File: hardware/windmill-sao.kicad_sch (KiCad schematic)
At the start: 0 parts

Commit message: Add space-sensitive components to the PCB
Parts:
- added J1: Conn_02x03_Counter_Clockwise, symbol Connector_Generic:Conn_02x03_Counter_Clockwise
- added J2: Conn_01x03, symbol Connector_Generic:Conn_01x03
- added LED1: WS2812B-2020, jlcpcb-parts:LED-SMD_4P-L2.0-W2.0-TL_WS2812B-2020, symbol jlcpcb-parts:WS2812B-2020

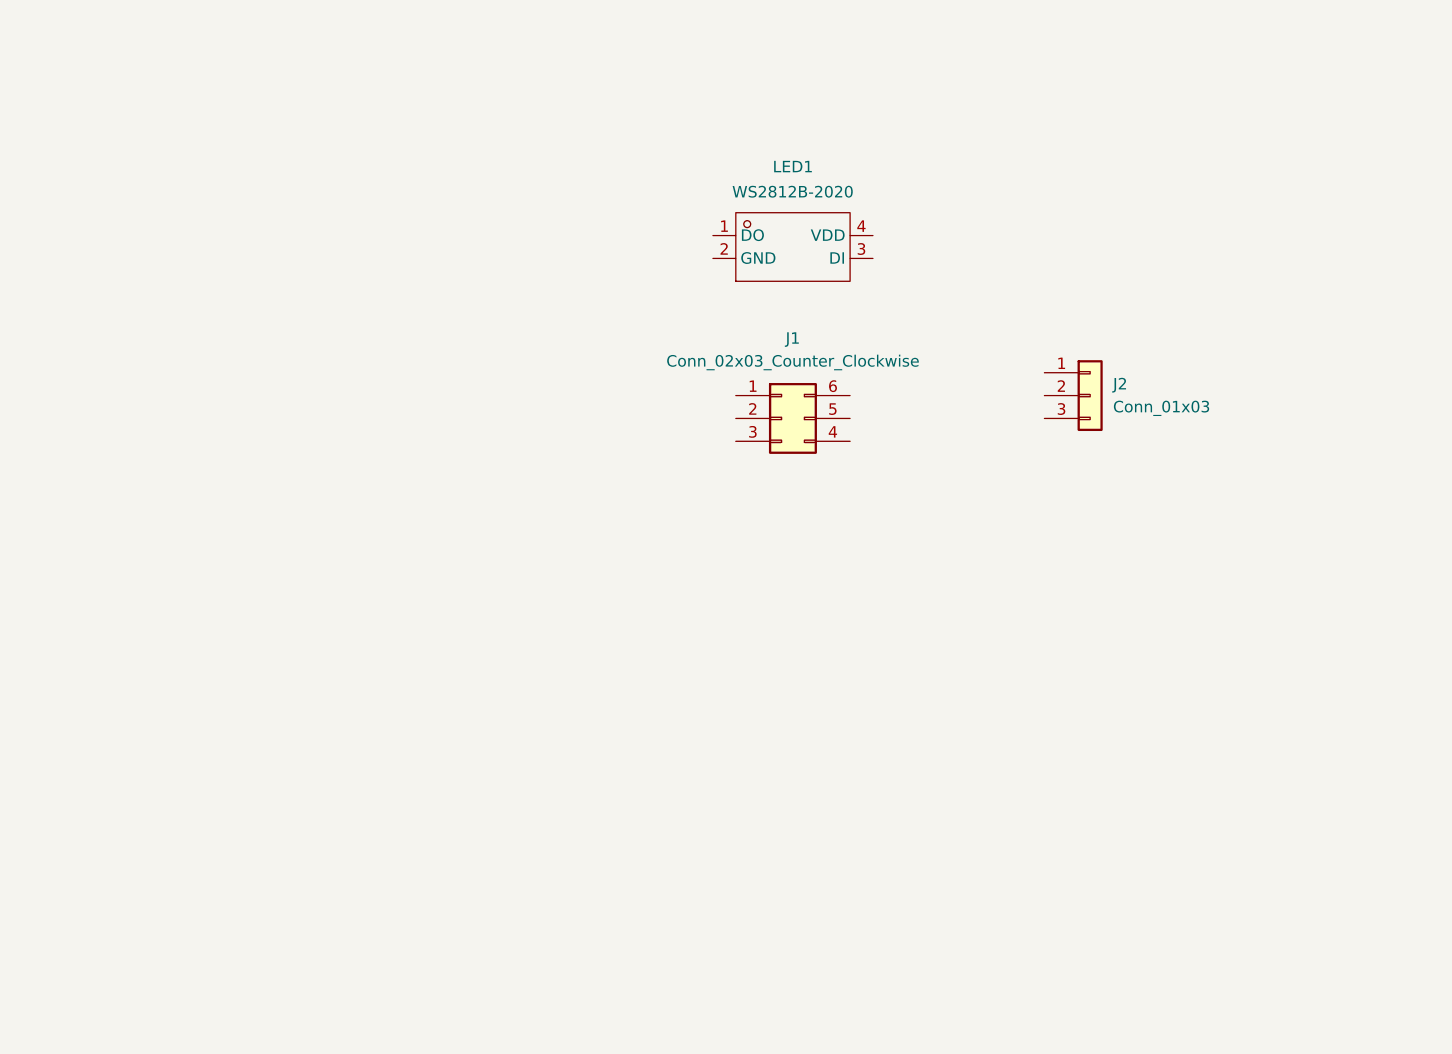
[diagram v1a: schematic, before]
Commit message: Add main PCB components
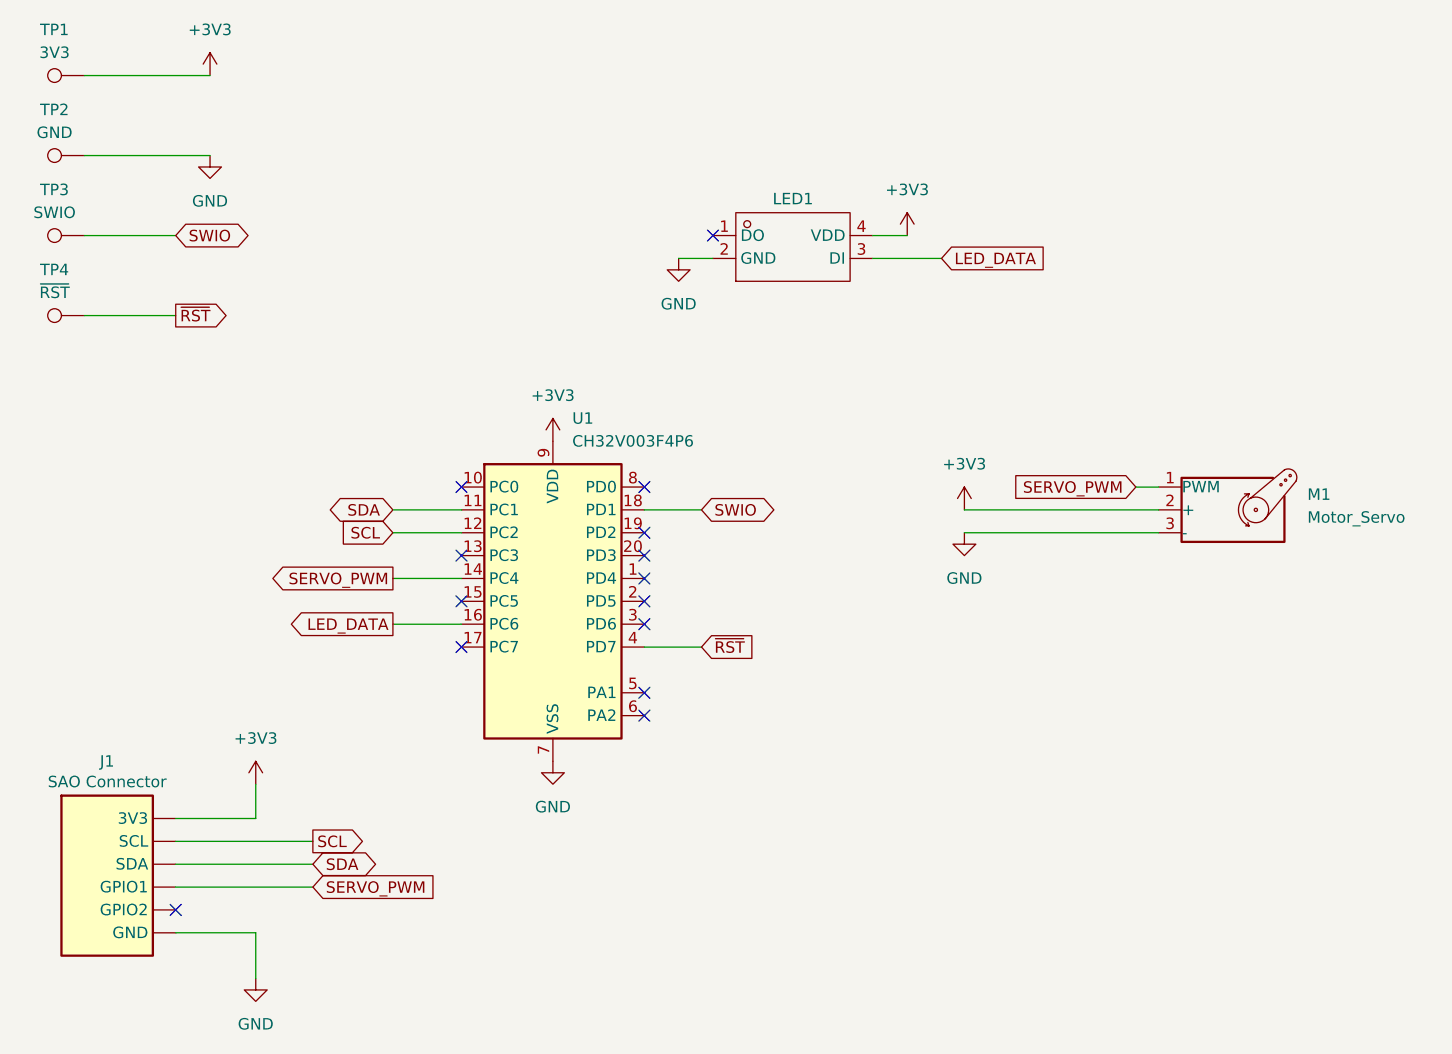
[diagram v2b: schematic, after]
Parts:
- added TP1: 3V3, TestPoint:TestPoint_Pad_D1.5mm, symbol Connector:TestPoint
- added TP2: GND, TestPoint:TestPoint_Pad_D1.5mm, symbol Connector:TestPoint
- added TP3: SWIO, TestPoint:TestPoint_Pad_D1.5mm, symbol Connector:TestPoint
- added TP4: ~{RST}, TestPoint:TestPoint_Pad_D1.5mm, symbol Connector:TestPoint
- added U1: CH32V003F4P6, Package_SO:TSSOP-20_4.4x6.5mm_P0.65mm, symbol MCU_WCH_RiscV:CH32V003FxPx
- J1: value Conn_02x03_Counter_Clockwise -> SAO Connector; footprint (none) -> kantoniak-kicad:SAO_Header_Addon_Side; symbol Connector_Generic:Conn_02x03_Counter_Clockwise -> kantoniak-kicad:Conn_SAO
- LED1: value WS2812B-2020 -> (none)
- M1: renamed from J2; value Conn_01x03 -> Motor_Servo; footprint (none) -> kantoniak-kicad:PinHeader_1x03_P2.54mm_Vertical_SG90; symbol Connector_Generic:Conn_01x03 -> Motor:Motor_Servo
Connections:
- net GND: now reaches J1.1 (GND)
- net GND: now also LED1.2 (GND), M1.3 (-), TP2.1, U1.7 (VSS)
- net SCL: now reaches J1.2 (SCL)
- net SCL: now also U1.12 (PC2)
- net SERVO_PWM: now reaches J1.4 (GPIO1)
- net SERVO_PWM: now also M1.1 (PWM), U1.14 (PC4)
- net SDA: now reaches J1.5 (SDA)
- net SDA: now also U1.11 (PC1)
- net +3V3: now reaches J1.6 (3V3)
- net +3V3: now also LED1.4 (VDD), M1.2 (+), TP1.1, U1.9 (VDD)
- net LED_DATA: now reaches LED1.3 (DI)
- net LED_DATA: now also U1.16 (PC6)
- new net SWIO: TP3.1, U1.18 (PD1)
- new net ~{RST}: TP4.1, U1.4 (PD7)
- no-connect marks 0 -> 14

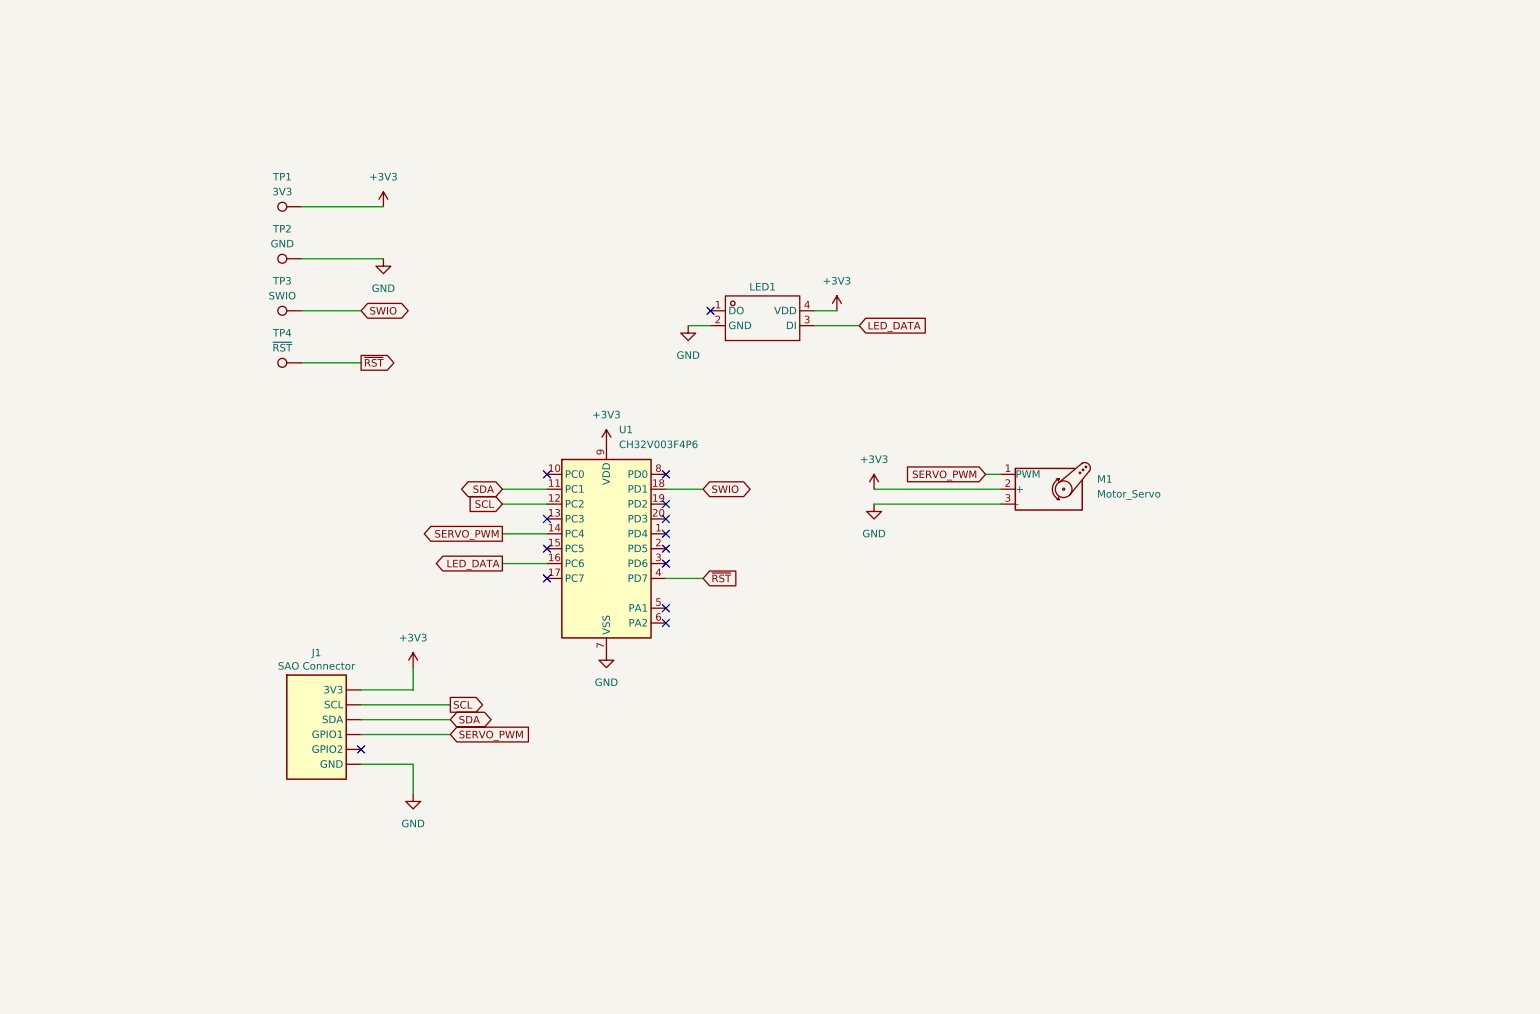
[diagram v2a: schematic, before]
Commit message: Add passives to the schematic, PCB WIP
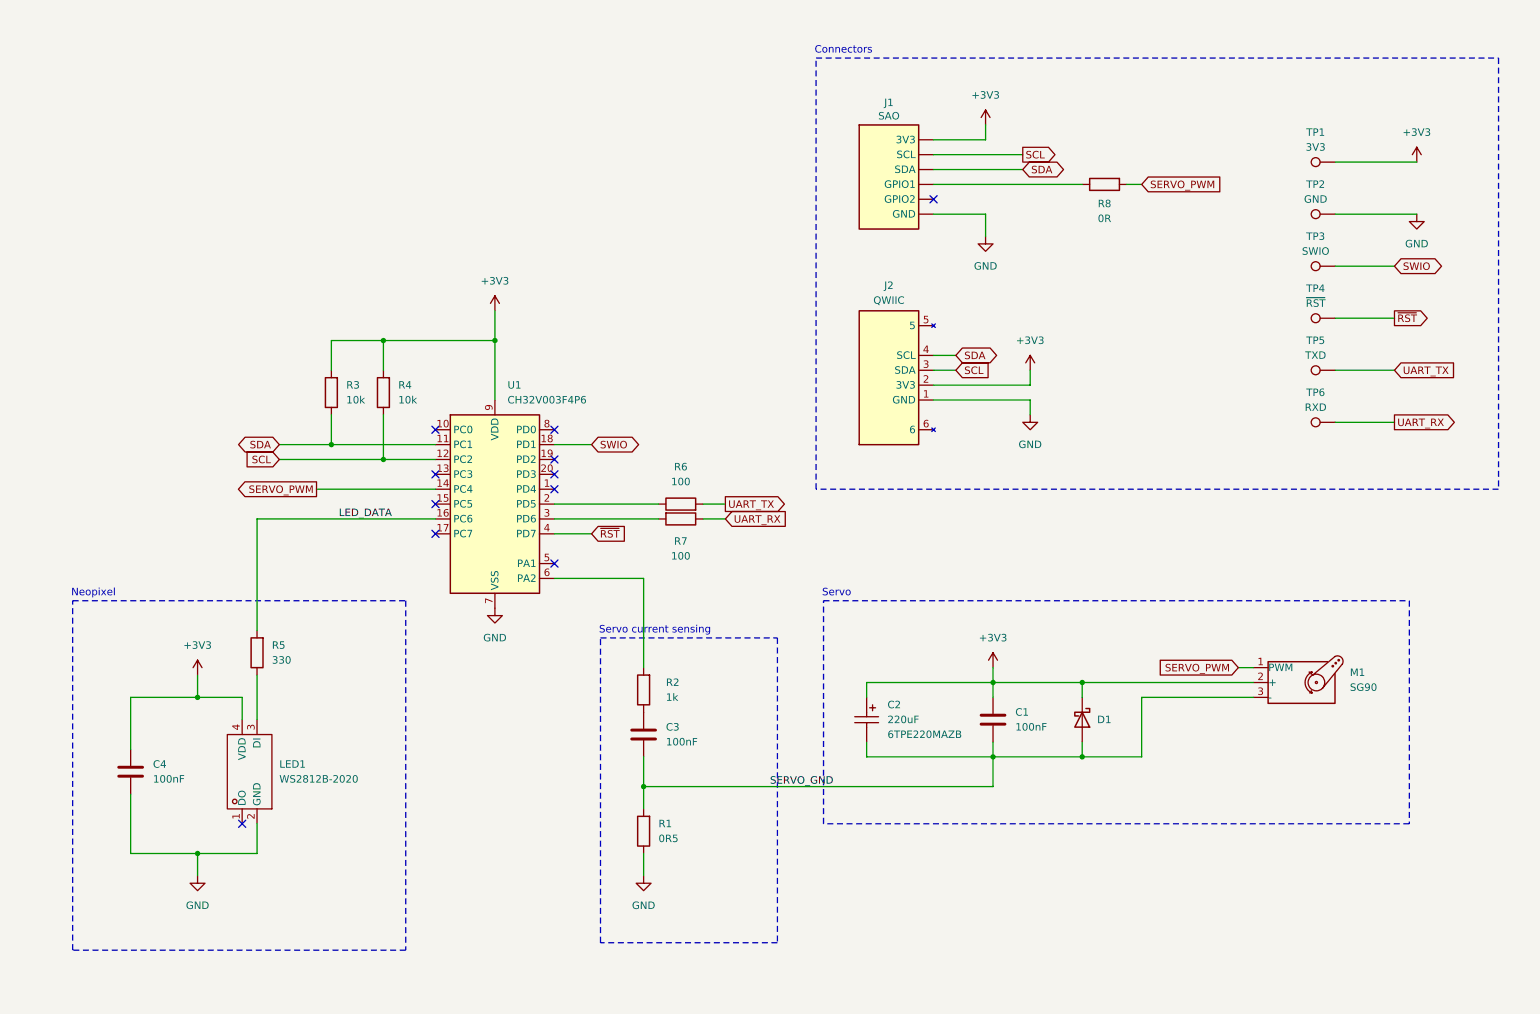
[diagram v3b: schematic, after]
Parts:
- added C1, C3, C4: 100nF, Capacitor_SMD:C_0201_0603Metric_Pad0.64x0.40mm_HandSolder, symbol Device:C
- added C2: 220uF, Capacitor_Tantalum_SMD:CP_EIA-3528-21_Kemet-B_HandSolder, symbol jlcpcb-parts:6TPE220MAZB
- added D1: D_Schottky, Diode_SMD:D_SMA, symbol Device:D_Schottky
- added J2: QWIIC, Connector_JST:JST_SH_SM04B-SRSS-TB_1x04-1MP_P1.00mm_Horizontal, symbol kantoniak-kicad:QWIIC
- added R1: 0R5, Capacitor_SMD:C_0201_0603Metric_Pad0.64x0.40mm_HandSolder, symbol Device:R
- added R2: 1k, Resistor_SMD:R_0201_0603Metric_Pad0.64x0.40mm_HandSolder, symbol Device:R
- added R3, R4: 10k, Resistor_SMD:R_0201_0603Metric_Pad0.64x0.40mm_HandSolder, symbol Device:R
- added R5: 330, Resistor_SMD:R_0201_0603Metric_Pad0.64x0.40mm_HandSolder, symbol Device:R
- added R6, R7: 100, Resistor_SMD:R_0201_0603Metric_Pad0.64x0.40mm_HandSolder, symbol Device:R
- added R8: 0R, Resistor_SMD:R_0201_0603Metric_Pad0.64x0.40mm_HandSolder, symbol Device:R
- added TP5: TXD, TestPoint:TestPoint_Pad_D1.5mm, symbol Connector:TestPoint
- added TP6: RXD, TestPoint:TestPoint_Pad_D1.5mm, symbol Connector:TestPoint
- J1: value SAO Connector -> SAO
- M1: value Motor_Servo -> SG90
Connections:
- net +3V3: now also C1.1, C2.1, C4.1, D1.1 (K), J2.2 (3V3), R3.2, R4.2
- net GND: now also C4.2, J2.1 (GND), R1.1; no longer M1.3 (-)
- net LED_DATA: now also R5.2; no longer LED1.3 (DI)
- net SCL: now also J2.3 (SDA), R4.1
- net SDA: now also J2.4 (SCL), R3.1
- net SERVO_PWM: now also R8.2; no longer J1.4 (GPIO1)
- net at U1.2 (PD5): now also R6.1
- net at U1.3 (PD6): now also R7.2
- net at U1.6 (PA2): now also R2.2
- new net: C3.1, R2.1
- new net: J1.4 (GPIO1), R8.1
- new net: LED1.3 (DI), R5.1
- new net SERVO_GND: C1.2, C2.2, C3.2, D1.2 (A), M1.3 (-), R1.2
- new net UART_RX: R7.1, TP6.1
- new net UART_TX: R6.2, TP5.1
- no-connect marks 14 -> 11
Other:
- note added: "Connectors"
- note added: "Neopixel"
- note added: "Servo"
- note added: "Servo current sensing"
- moved on the sheet: J1, LED1, M1, TP1, TP2, TP3, TP4, U1

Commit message: Add configuration resistors, route the PCB
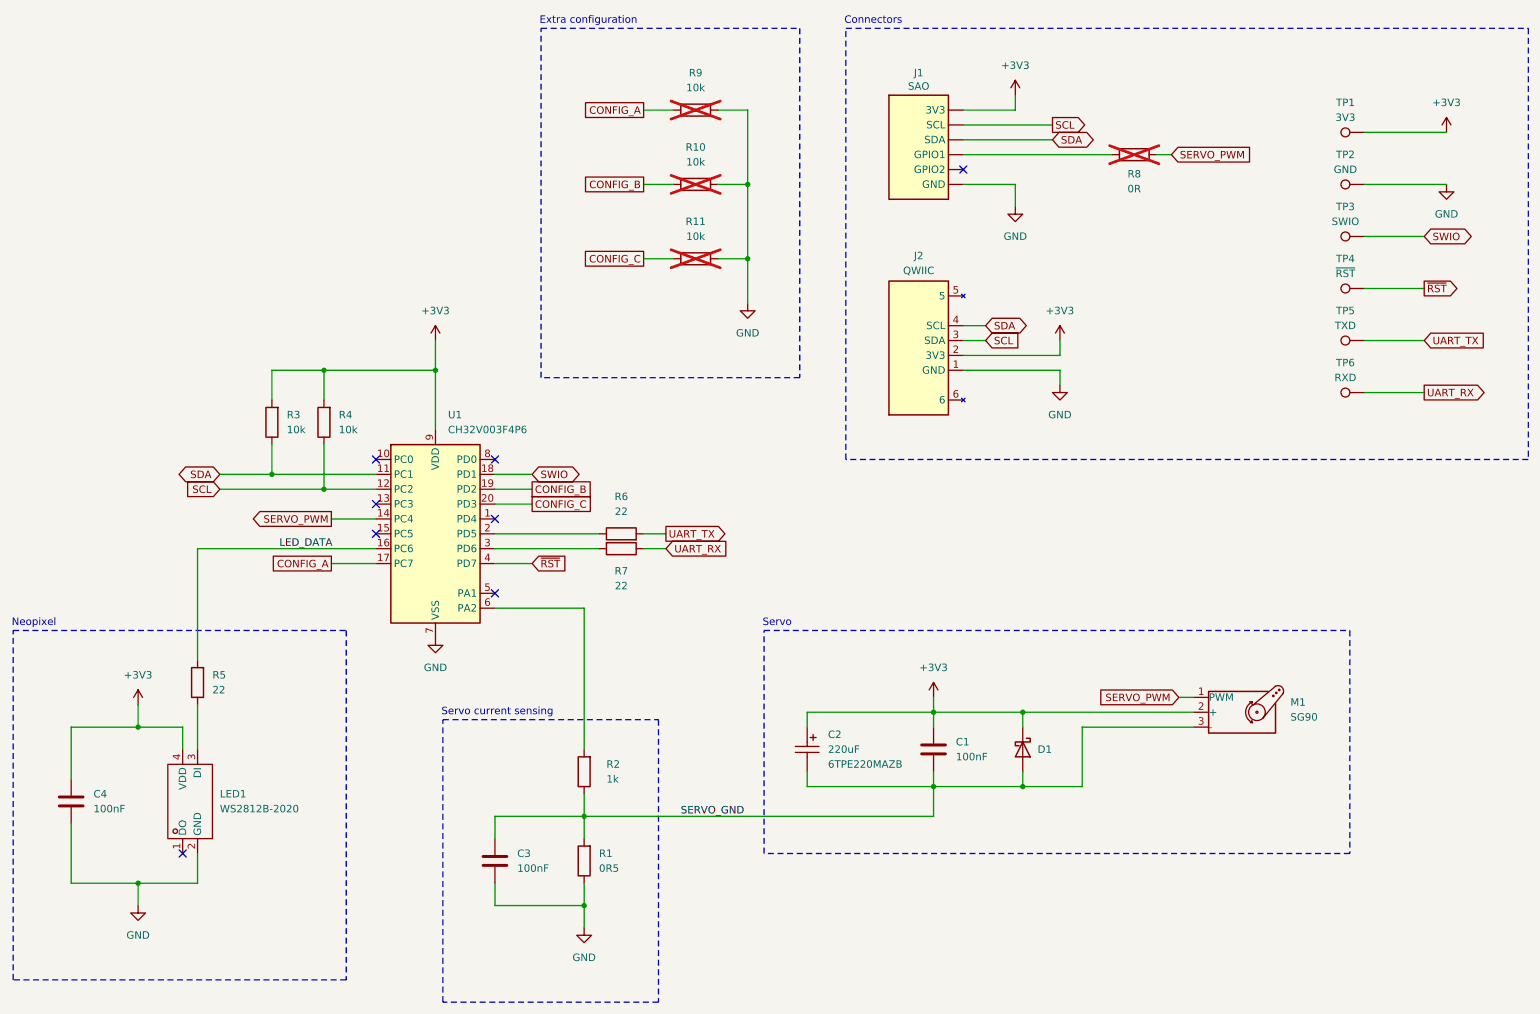
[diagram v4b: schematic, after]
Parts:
- added R10, R11, R9: 10k, Resistor_SMD:R_0603_1608Metric_Pad0.98x0.95mm_HandSolder, symbol Device:R
- C1, C3, C4: footprint Capacitor_SMD:C_0201_0603Metric_Pad0.64x0.40mm_HandSolder -> Capacitor_SMD:C_0603_1608Metric_Pad1.08x0.95mm_HandSolder
- R1: footprint Capacitor_SMD:C_0201_0603Metric_Pad0.64x0.40mm_HandSolder -> Resistor_SMD:R_1206_3216Metric_Pad1.30x1.75mm_HandSolder
- R2, R3, R4: footprint Resistor_SMD:R_0201_0603Metric_Pad0.64x0.40mm_HandSolder -> Resistor_SMD:R_0603_1608Metric_Pad0.98x0.95mm_HandSolder
- R5: value 330 -> 22; footprint Resistor_SMD:R_0201_0603Metric_Pad0.64x0.40mm_HandSolder -> Resistor_SMD:R_0603_1608Metric_Pad0.98x0.95mm_HandSolder
- R6, R7: value 100 -> 22; footprint Resistor_SMD:R_0201_0603Metric_Pad0.64x0.40mm_HandSolder -> Resistor_SMD:R_0603_1608Metric_Pad0.98x0.95mm_HandSolder
- R8: footprint Resistor_SMD:R_0201_0603Metric_Pad0.64x0.40mm_HandSolder -> Resistor_SMD:R_0603_1608Metric_Pad0.98x0.95mm_HandSolder; now not fitted
- TP1, TP2, TP3, TP4, TP5, TP6: now left out of the parts list
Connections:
- net GND: now also C3.2, R10.1, R11.1, R9.2
- net SERVO_GND: now also C3.1, R2.1; no longer C3.2
- net CONFIG_A: now reaches U1.17 (PC7)
- net CONFIG_A: now also R9.1
- net CONFIG_B: now reaches U1.19 (PD2)
- net CONFIG_B: now also R10.2
- net CONFIG_C: now reaches U1.20 (PD3)
- net CONFIG_C: now also R11.2
- no-connect marks 11 -> 8
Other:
- note added: "Extra configuration"
- company: (none) -> @kantoniak
- title: (none) -> Windmill SAO
- moved on the sheet: C1, C2, C3, C4, D1, J1, J2, LED1, M1, R1, R2, R3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
